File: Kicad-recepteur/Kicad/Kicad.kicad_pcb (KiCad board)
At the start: 4 copper layers, 32 x 28.2 mm, 25 parts, among them J1 Conn_02x07_Odd_Even, J2 Conn_01x02, J3 Conn_01x04, J4 Conn_01x02, J42 Conn_01x04, U1 STM32L021K4Tx, U2 BU33SD5WG-TR

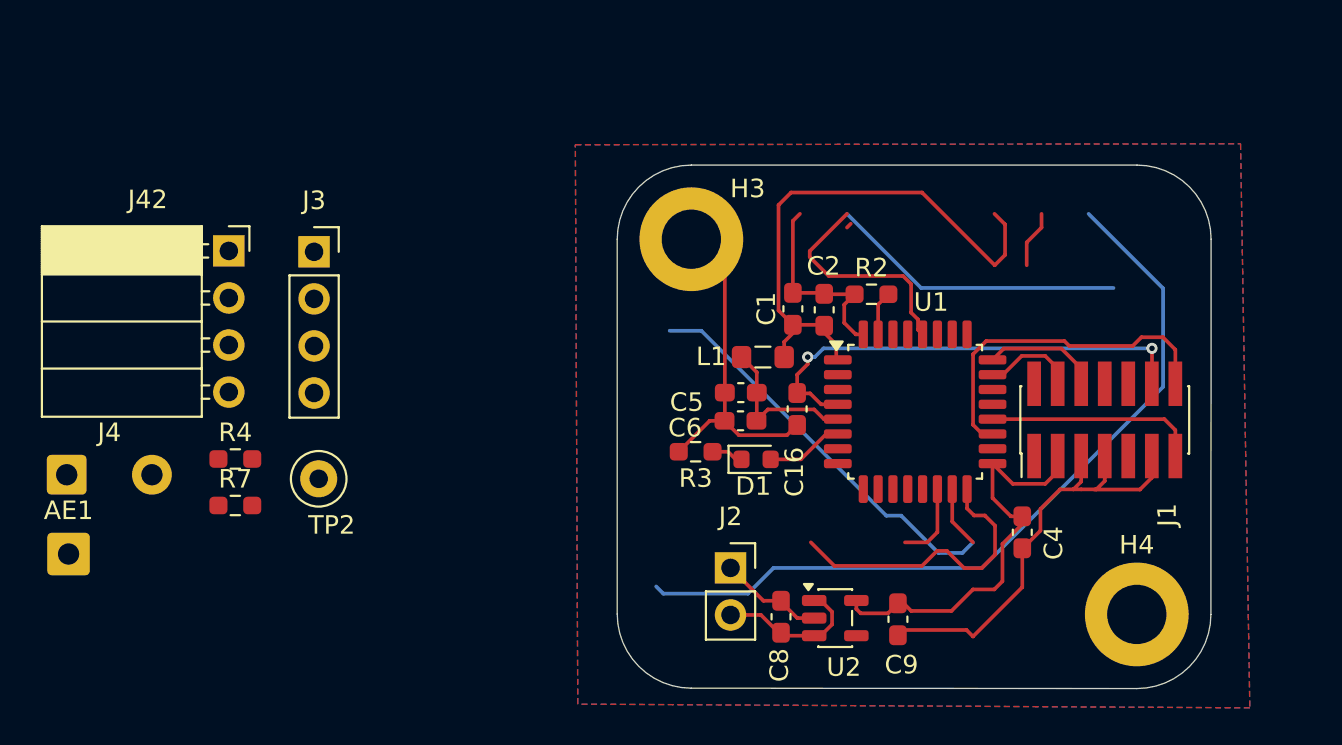
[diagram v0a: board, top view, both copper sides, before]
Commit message: feat: Initial KiCad PCB layout and project files for the receiver module.
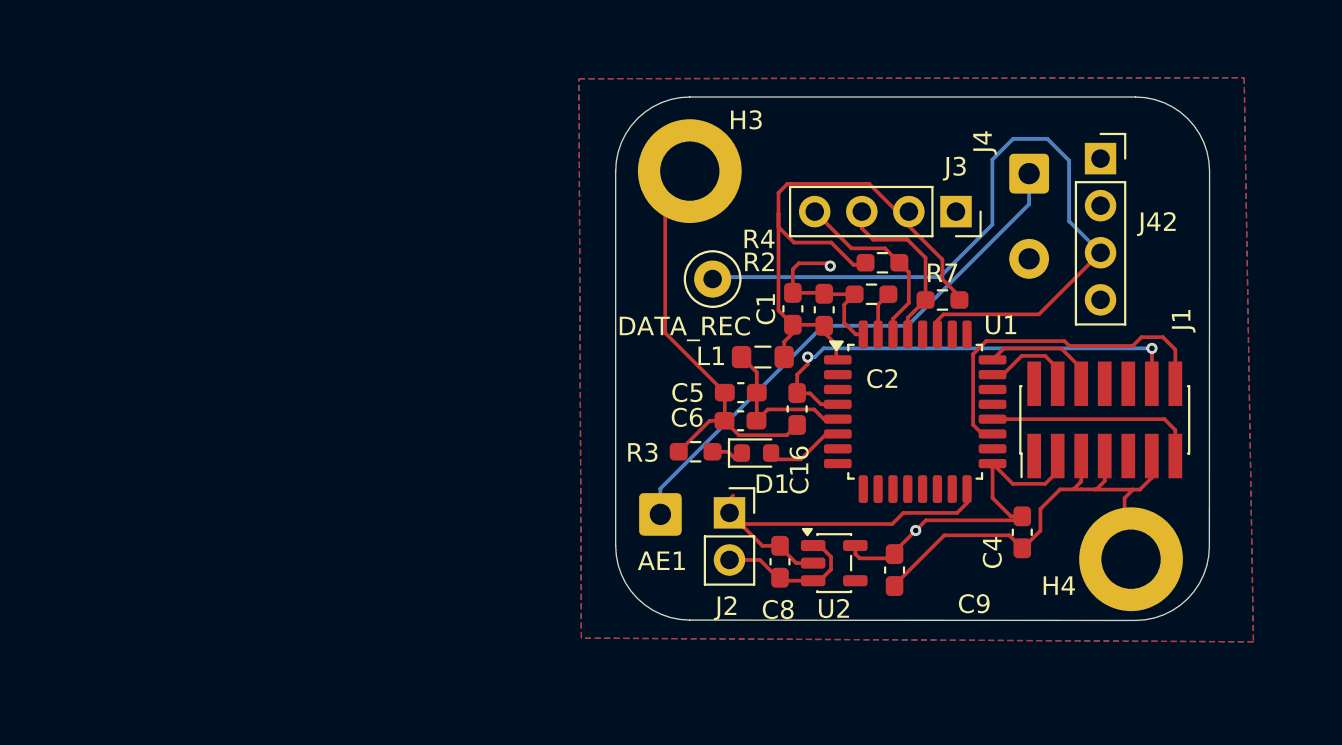
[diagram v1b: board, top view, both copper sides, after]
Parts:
- J42: footprint Connector_PinSocket_2.54mm:PinSocket_1x04_P2.54mm_Horizontal -> Connector_PinSocket_2.54mm:PinSocket_1x04_P2.54mm_Vertical
- moved J4 54.4 mm to (117.7, 93.4), turned to -90 degrees
- moved J42 47.3 mm to (121.6, 92.6)
- moved R7 39.7 mm to (113.0, 100.2)
- moved R4 36.5 mm to (109.8, 98.2)
- moved J3 34.7 mm to (113.8, 95.5), turned to -90 degrees
- moved AE1 32.0 mm to (97.8, 111.8)
- moved DATA_REC 23.8 mm to (100.6, 99.1)
- moved H3 3.68 mm to (99.4, 93.3)
- moved H4 3.00 mm to (123.2, 114.2)
- moved U2 2.97 mm to (107.2, 114.5)
- moved C8 2.97 mm to (104.3, 114.4)
- moved J2 2.97 mm to (101.5, 111.7)
- moved C9 2.66 mm to (110.4, 114.8)
- moved D1 0.34 mm to (103.0, 108.5)
- renumbered TP2 to DATA_REC
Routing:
- net (no net): track 81.0 -> 0.00 mm
- net DATA_REC: track 0.00 -> 41.7 mm
- net Net-(AE1-A): track 0.00 -> 29.3 mm
- net unconnected-(U1-PB5-Pad28): track 12.2 -> 0.00 mm
- net SDA: track 0.00 -> 10.1 mm
- net SCL: track 0.00 -> 9.53 mm
- net unconnected-(U1-PB0-Pad14): track 4.30 -> 0.00 mm
- net unconnected-(U1-PB1-Pad15): track 3.34 -> 0.00 mm
- net GND: track 80.3 -> 82.8 mm, vias 0 -> 1
- net +3.3V: track 52.3 -> 53.1 mm, vias 0 -> 1
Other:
- board size 32 x 28.2 mm -> 32.1 x 28.2 mm

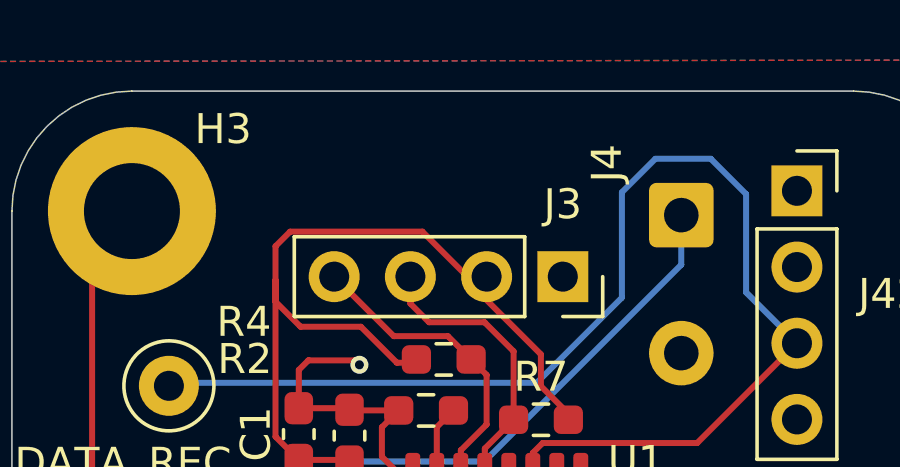
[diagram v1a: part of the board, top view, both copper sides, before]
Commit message: refactor: Reorganize Kicad project files into a `Kicad-recepteur` subfolder, including a new PCB layout, and add a `.gitignore`.
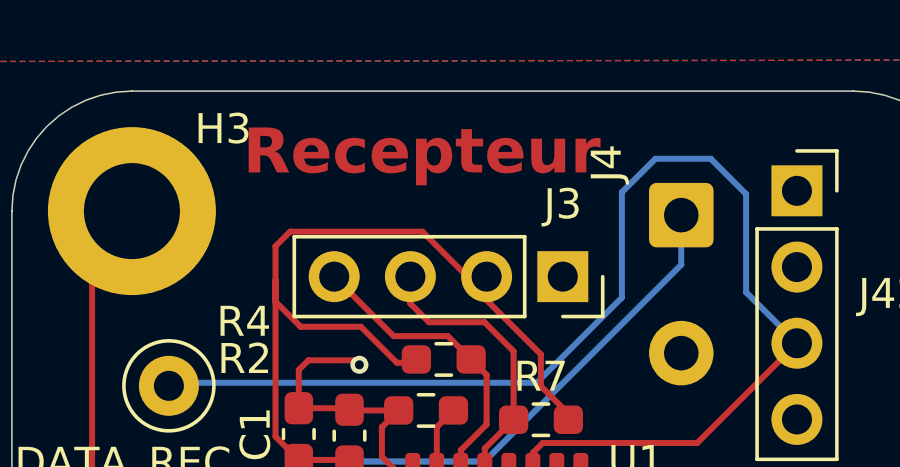
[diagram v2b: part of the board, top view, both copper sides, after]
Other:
- board text added: "Recepteur"
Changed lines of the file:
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@@
 		(layer "Edge.Cuts")
+	)
+	(gr_text "Recepteur"
+		(at 103.1 92.19 0)
+		(layer "F.Cu")
+		(effects
+			(font
+				(size 1.5 1.5)
+				(thickness 0.3)
+				(bold yes)
+			)
+			(justify left bottom)
+		)
 	)
 	(segment

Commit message: feat: Add initial KiCad PCB and schematic files for the receiver project.
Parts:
- removed J2: Conn_01x02, Connector_PinSocket_2.54mm:PinSocket_1x02_P2.54mm_Vertical
- added J5: USB_C_Receptacle_PowerOnly_6P, Connector_USB:USB_C_Receptacle_GCT_USB4125-xx-x-0190_6P_TopMnt_Horizontal, F.Cu at (101.2, 115.1)
- added R1: 5.1k, Resistor_SMD:R_0603_1608Metric_Pad0.98x0.95mm_HandSolder, F.Cu at (103.8, 110.0)
- added R5: 5.1k, Resistor_SMD:R_0603_1608Metric_Pad0.98x0.95mm_HandSolder, F.Cu at (100.1, 110.0)
- moved AE1 31.0 mm to (125.6, 98.1)
- moved C9 3.40 mm to (113.8, 114.1)
- moved U2 3.26 mm to (110.4, 114.4)
- moved C8 3.26 mm to (107.5, 114.4), turned to 90 degrees
- renumbered DATA_REC to TP2
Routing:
- net Net-(AE1-A): track 29.3 -> 11.8 mm
- net +3.3V: track 53.1 -> 67.4 mm
- net GND: track 82.8 -> 95.0 mm
- net +5V: track 8.09 -> 16.3 mm
- net Net-(J5-CC1): track 0.00 -> 2.65 mm
- net Net-(J5-CC2): track 0.00 -> 2.52 mm
- removed copper zone on B.Cu, net (none)
- removed copper zone on F.Cu, net (none)
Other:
- board size 32.1 x 28.2 mm -> 32.1 x 29.9 mm

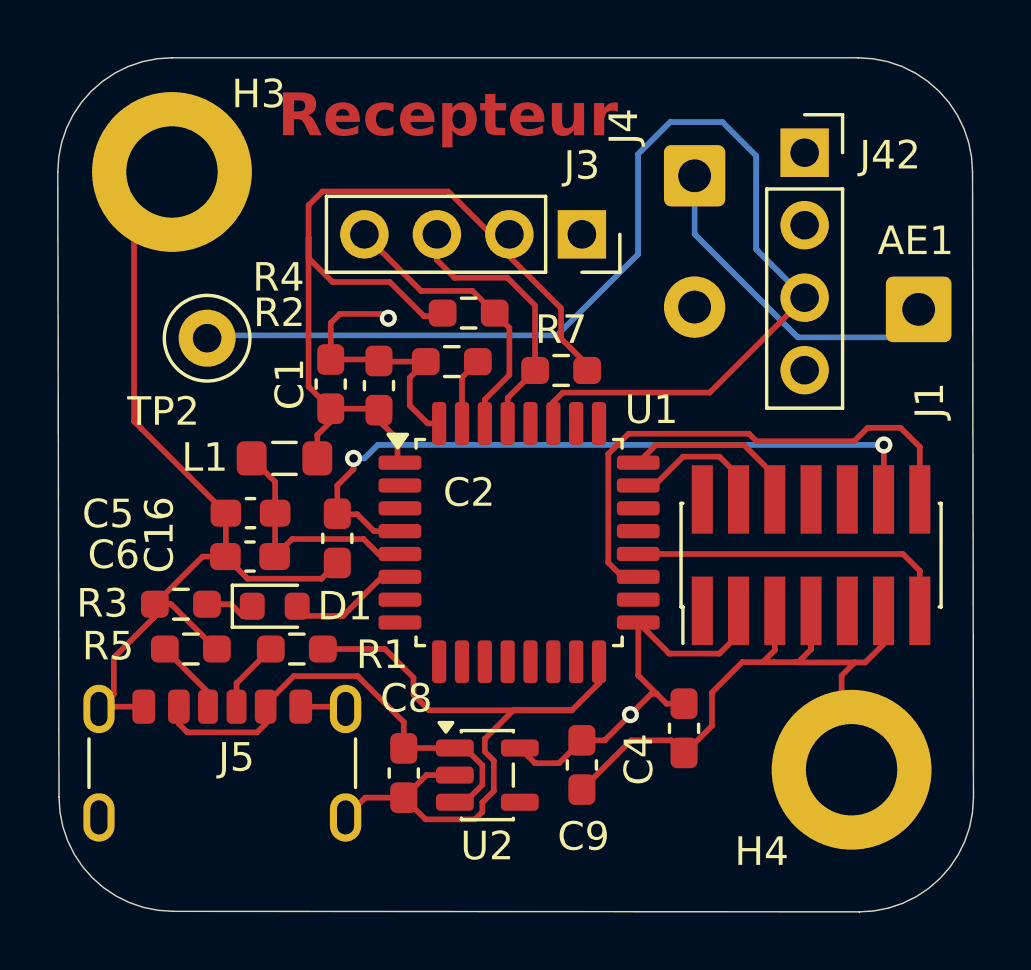
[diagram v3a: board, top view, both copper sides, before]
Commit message: feat: Add initial KiCad project files for emitter and receiver modules.
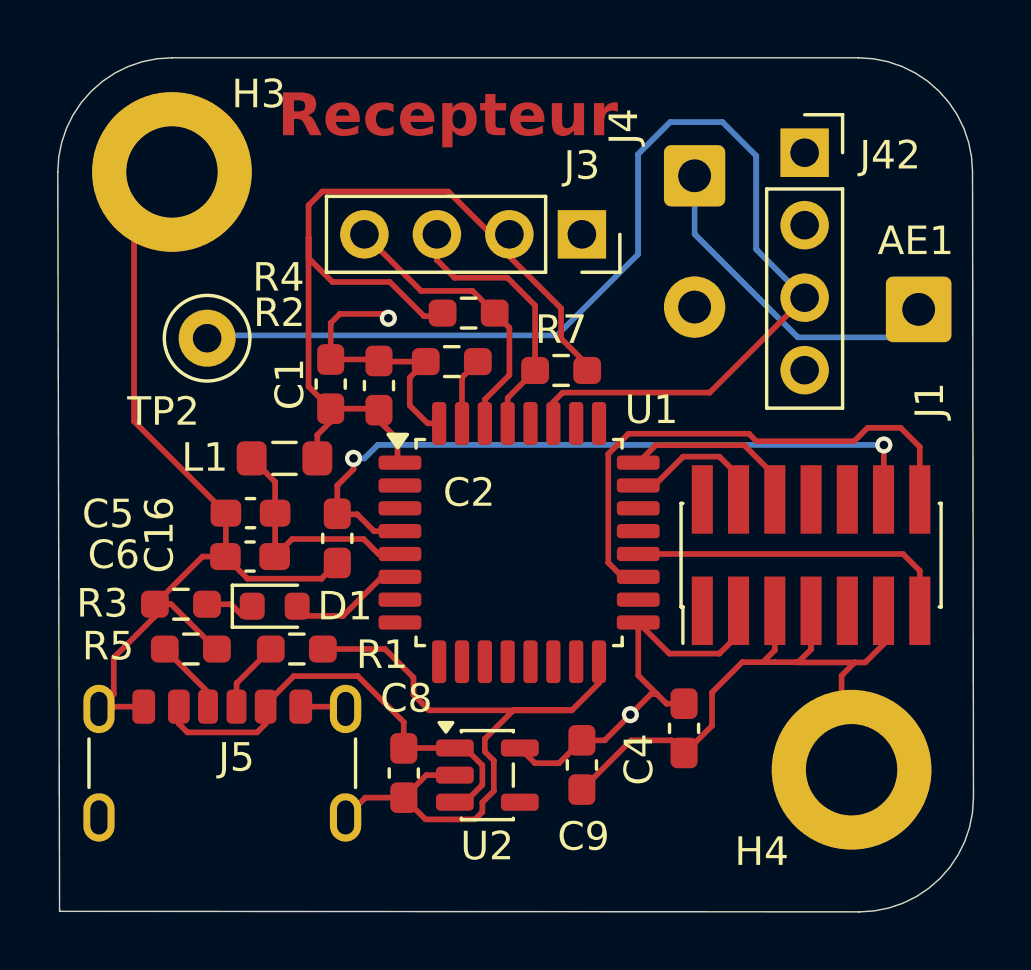
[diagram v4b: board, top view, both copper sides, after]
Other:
- outline, holes or cut-outs redrawn
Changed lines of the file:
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@@
 	(gr_line
 		(start 123.48 119.22)
-		(end 99.44 119.2)
+		(end 95.46 119.2)
 		(stroke
 			(width 0.05)
@@
 	)
 	(gr_arc
-		(start 99.44 119.2)
-		(mid 96.611573 118.028427)
-		(end 95.44 115.2)
-		(stroke
-			(width 0.05)
-			(type default)
-		)
-		(layer "Edge.Cuts")
-	)
-	(gr_arc
 		(start 95.3975 93.295)
 		(mid 96.569073 90.466573)
@@
 	)
 	(gr_line
-		(start 95.44 115.2)
+		(start 95.46 119.2)
 		(end 95.3975 93.295)
 		(stroke

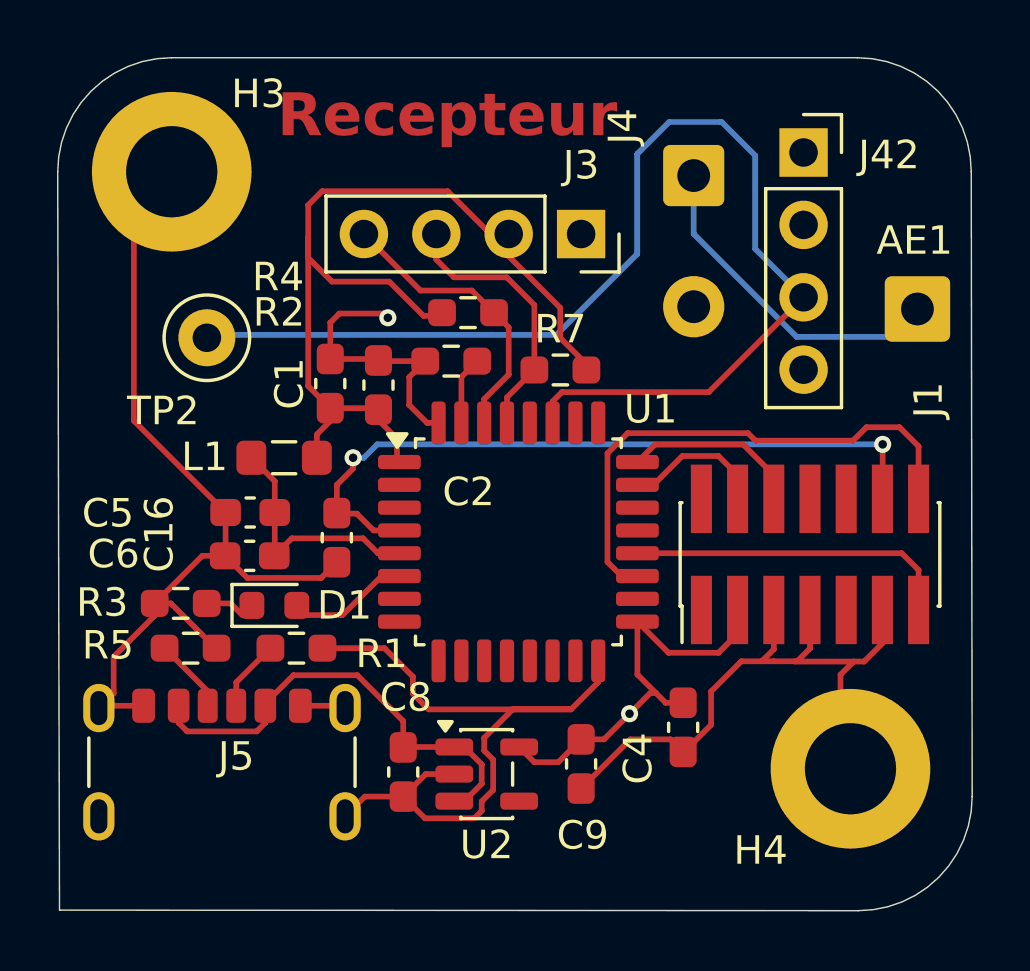
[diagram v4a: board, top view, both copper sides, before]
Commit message: feat: Add initial Kicad PCB designs for receiver and emitter, and generate emitter Gerber files.
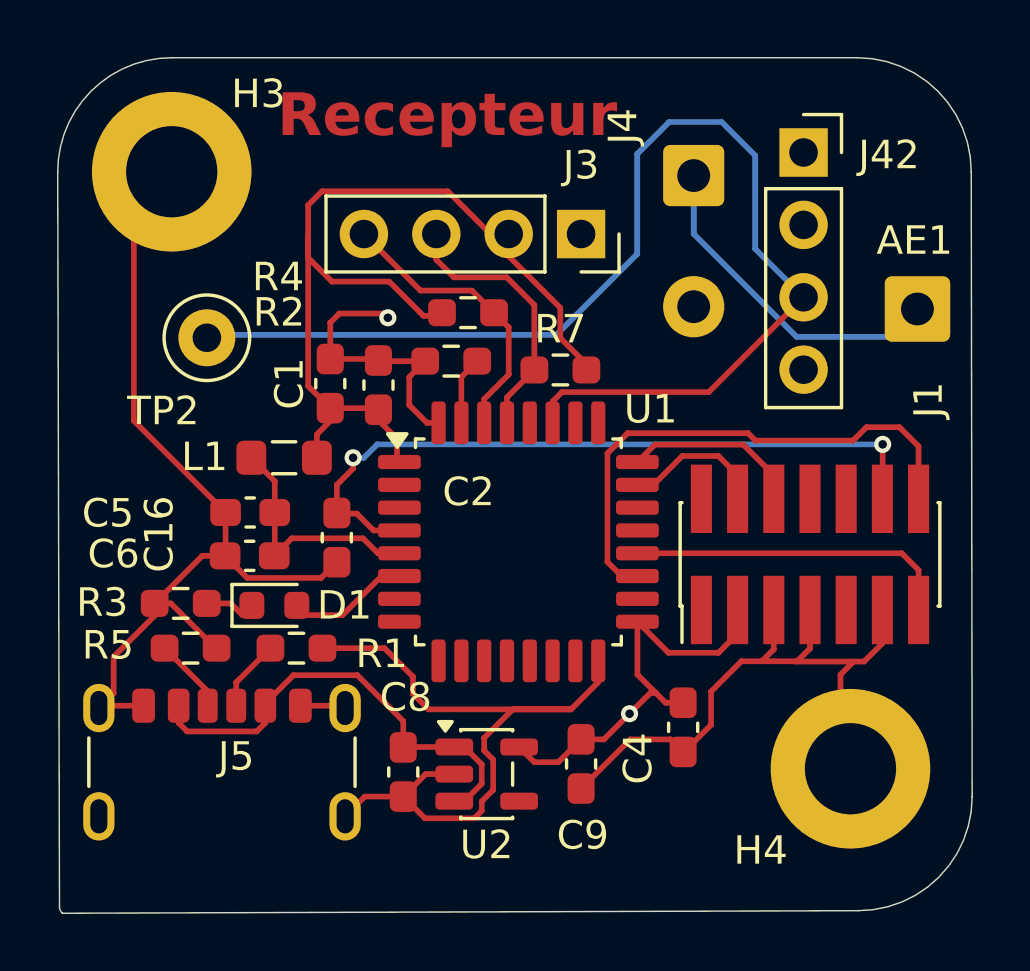
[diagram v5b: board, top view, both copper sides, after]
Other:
- board size 32.1 x 29.9 mm -> 32.1 x 30 mm
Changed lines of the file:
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@@
 	(gr_line
 		(start 123.48 119.22)
-		(end 95.46 119.2)
+		(end 95.56 119.31)
 		(stroke
 			(width 0.05)
@@
 	)
 	(gr_arc
-		(start 95.3975 93.295)
-		(mid 96.569073 90.466573)
+		(start 95.397501 93.31)
+		(mid 96.563765 90.471879)
 		(end 99.3975 89.295)
 		(stroke
@@
 		(layer "Edge.Cuts")
 	)
-	(gr_line
-		(start 95.46 119.2)
-		(end 95.3975 93.295)
+	(gr_arc
+		(start 95.56 119.31)
+		(mid 95.493772 119.218114)
+		(end 95.46 119.11)
 		(stroke
 			(width 0.05)
+			(type default)
+		)
+		(layer "Edge.Cuts")
+	)
+	(gr_line
+		(start 95.397501 93.309966)
+		(end 95.46 119.11)
+		(stroke
+			(width 0.05)
